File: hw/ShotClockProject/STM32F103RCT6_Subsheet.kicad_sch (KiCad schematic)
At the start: 40 parts, among them J1 USB_C_Receptacle_USB2.0, J2 Conn_ST_STDC14, J3 Conn_01x06_Pin, Q1 Q_NPN_BCE, SW1 SW_SPDT, U1 STM32F103RCT6, U2 LD39015M33R, Y1 16MHz

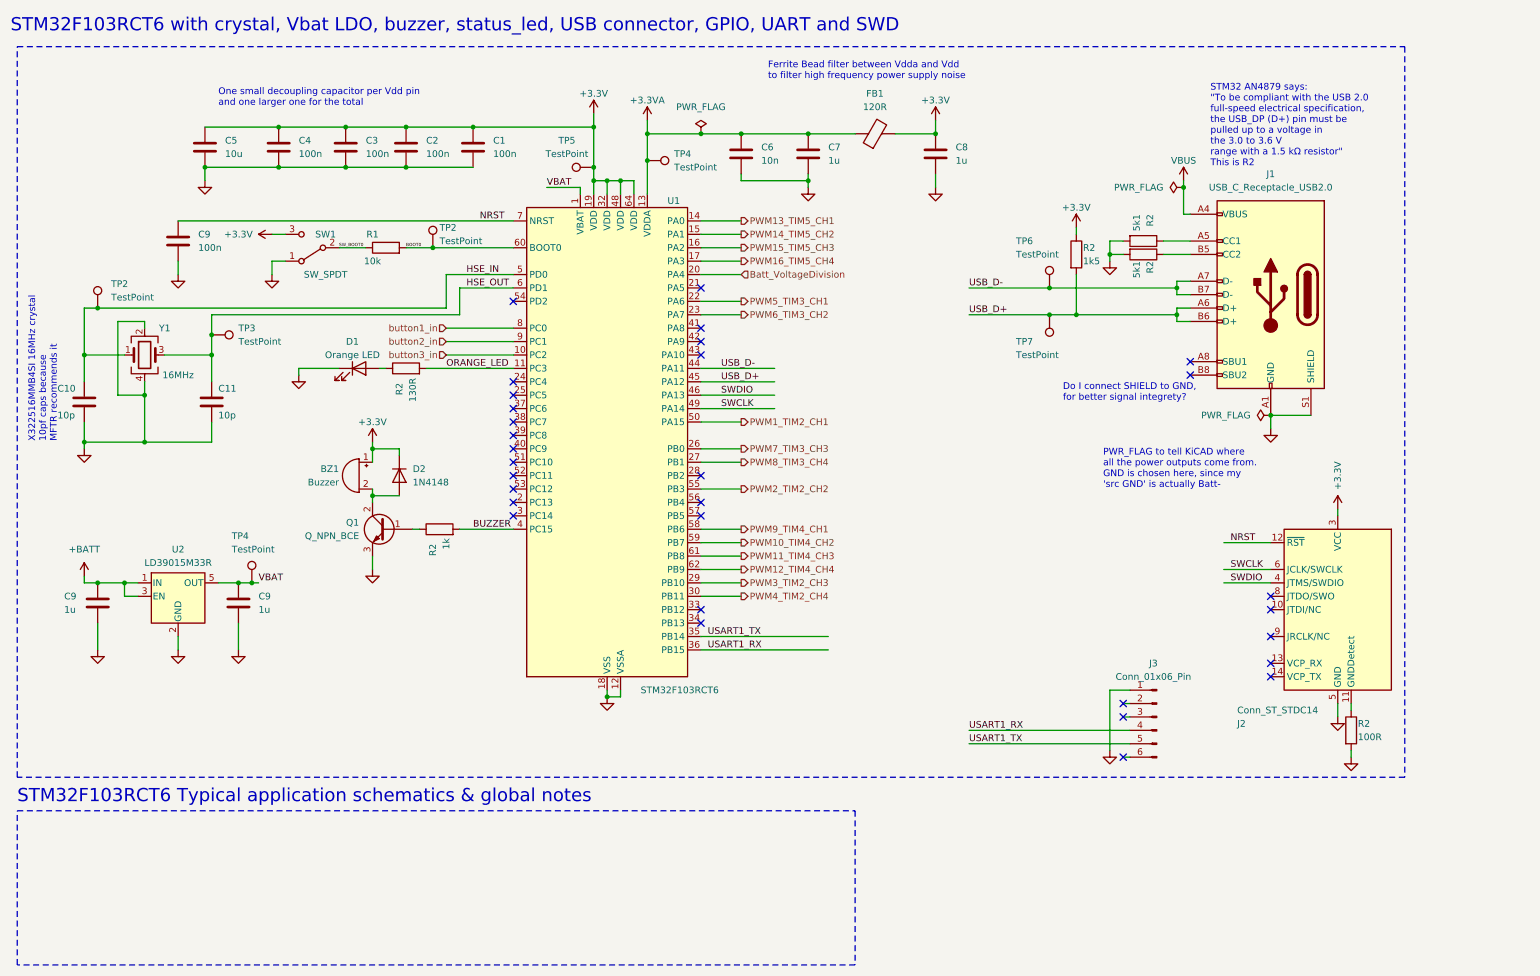
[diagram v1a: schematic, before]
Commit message: Changes headers, usb schematic and footprint
Now using standing USBc
Header & header pins are imported
All have 3d models now.

Removed fp-info-cache and added it to gitignore
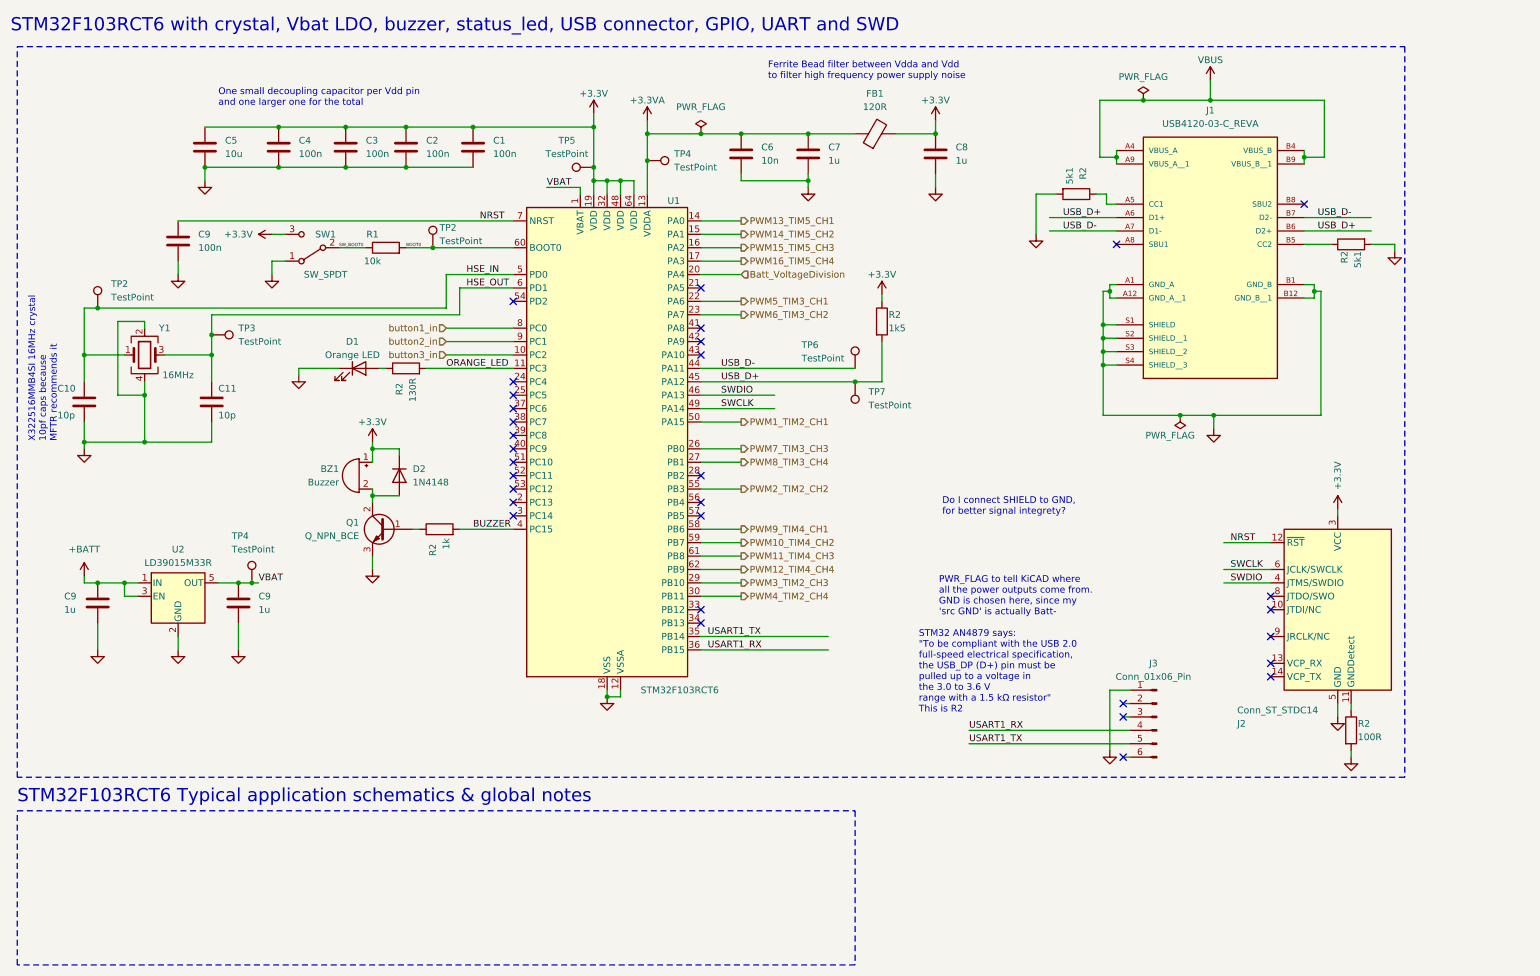
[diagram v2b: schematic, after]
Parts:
- removed J1: USB_C_Receptacle_USB2.0, Connector_USB:USB_C_Receptacle_Molex_105450-0101, symbol Connector:USB_C_Receptacle_USB2.0
- added J1: USB4120-03-C_REVA, USB4120-03-C:GCT_USB4120-03-C_REVA_With3DModel, symbol USB4120-03-C_REVA:USB4120-03-C_REVA
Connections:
- net GND: now also J1.A1 (GND_A), J1.A12 (GND_A__1), J1.B1 (GND_B), J1.B12 (GND_B__1), J1.S1 (SHIELD), J1.S2 (SHIELD__1), J1.S3 (SHIELD__2), J1.S4 (SHIELD__3)
- net USB_D+: now also J1.A6 (D1+), J1.B6 (D2+)
- net USB_D-: now also J1.A7 (D1-), J1.B7 (D2-)
- net VBUS: now also J1.A4 (VBUS_A), J1.A9 (VBUS_A__1), J1.B4 (VBUS_B), J1.B9 (VBUS_B__1)
- net at R2.1: now also J1.A5 (CC1)
- net at R2.1: now also J1.B5 (CC2)
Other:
- moved on the sheet: R2, TP6, TP7

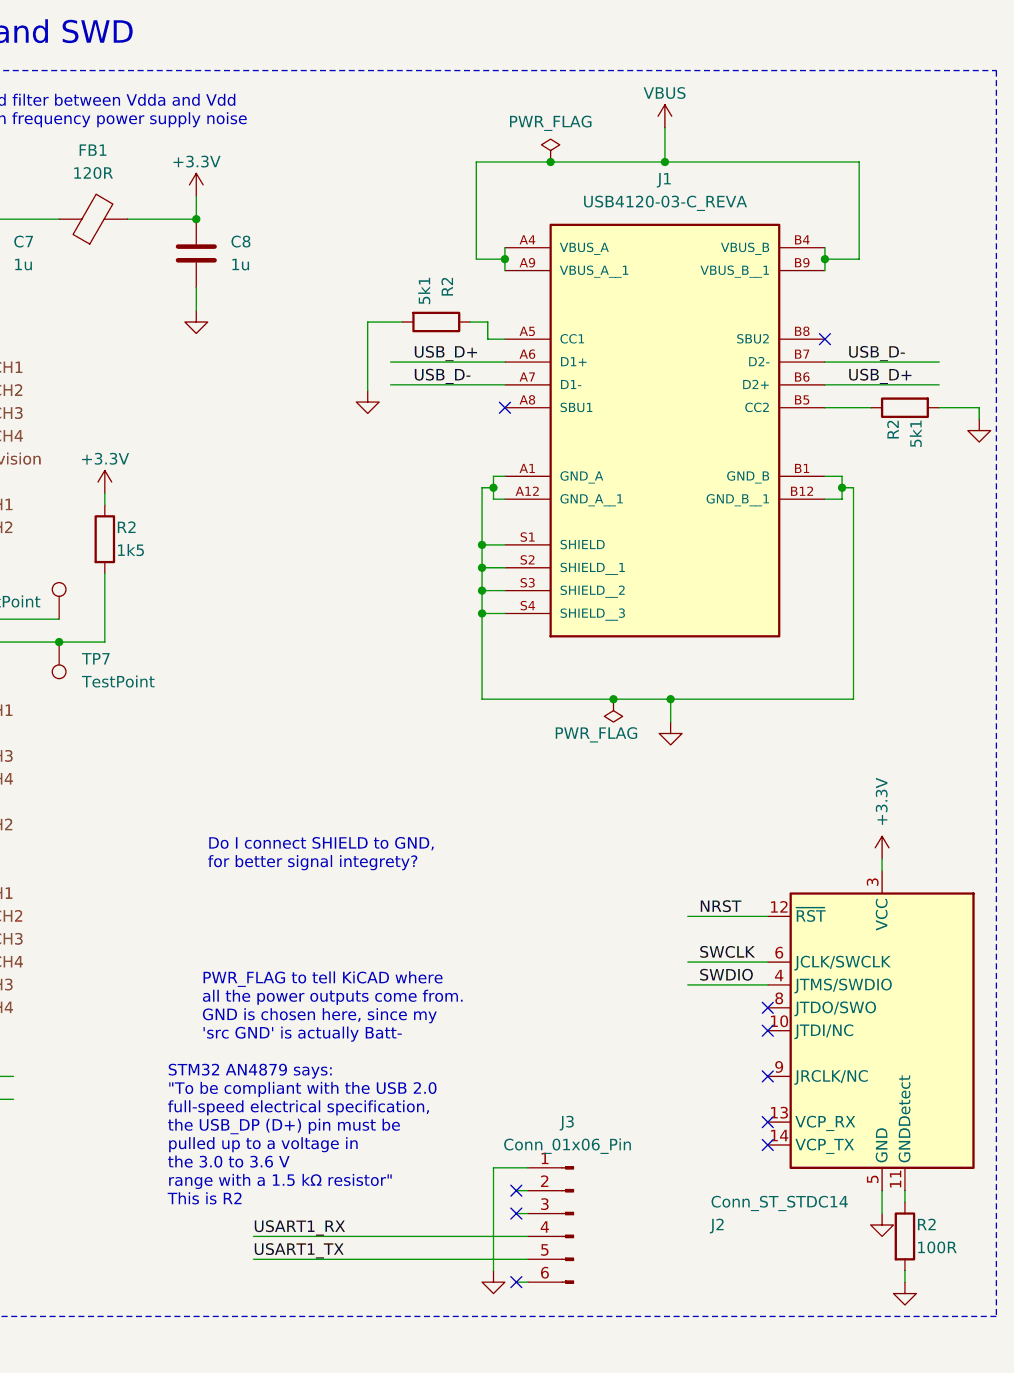
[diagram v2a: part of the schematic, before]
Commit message: Finished rough layout of PCB (ready for review)
Changed battery polarity to match the batteries I have.
Added power led to voltage regulator
Removed old comments from schematic
Gave all footprints a 3D model
Replaced batttery footprint with a SMD JST 3 pins horizontal connector
Finished rough placement of components
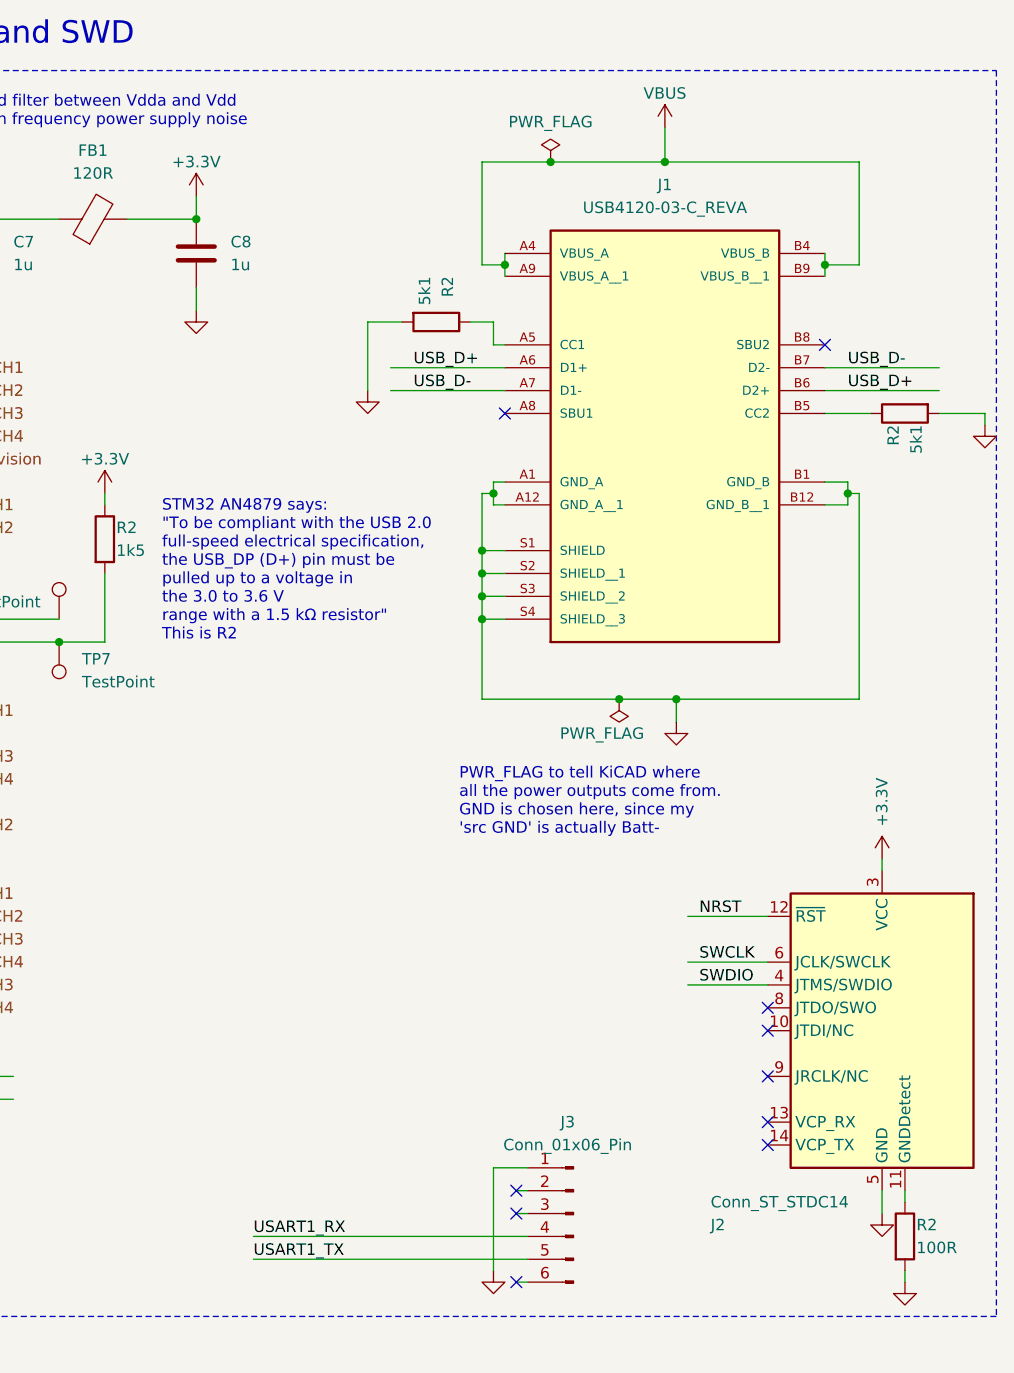
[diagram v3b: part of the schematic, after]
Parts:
- J2: footprint Connector_PinHeader_1.27mm:PinHeader_2x07_P1.27mm_Horizontal -> Connector_PinHeader_1.27mm:PinHeader_2x07_P1.27mm_Vertical_SMD
- SW1: footprint Button_Switch_SMD:SW_SPDT_PCM12 -> Button_Switch_SMD_Altered:SW_SPDT_PCM12_Upwards
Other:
- note removed: "Do I connect SHIELD to GND, for better signal integrety?"
- moved on the sheet: J1, R2

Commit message: First feedback round from Luc on schematic
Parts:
- added R2: 1k, Resistor_SMD:R_0402_1005Metric, symbol Device:R
- C10, C11: value 10p -> 6p
- R2: value 1k -> 300R
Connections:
- net GND: now also R2.1
- net at Q1.1 (B), R2.1: now also R2.2
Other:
- note added: "CL = ((CX1 x CX2) / (CX1 + CX2)) + Cstray"
- note removed: "X322516MMB4SI 16MHz crystal 10pf caps because MFTR recommends it"
- moved on the sheet: BZ1, D2, Q1
